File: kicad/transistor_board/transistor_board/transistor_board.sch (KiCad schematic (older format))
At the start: 16 parts, among them Q1 MMBF170, Q2 MMBF170, Q3 MMBF170, U1 DRV8872DDAR, U2 ESP32-cam, U3 LM7805_TO220

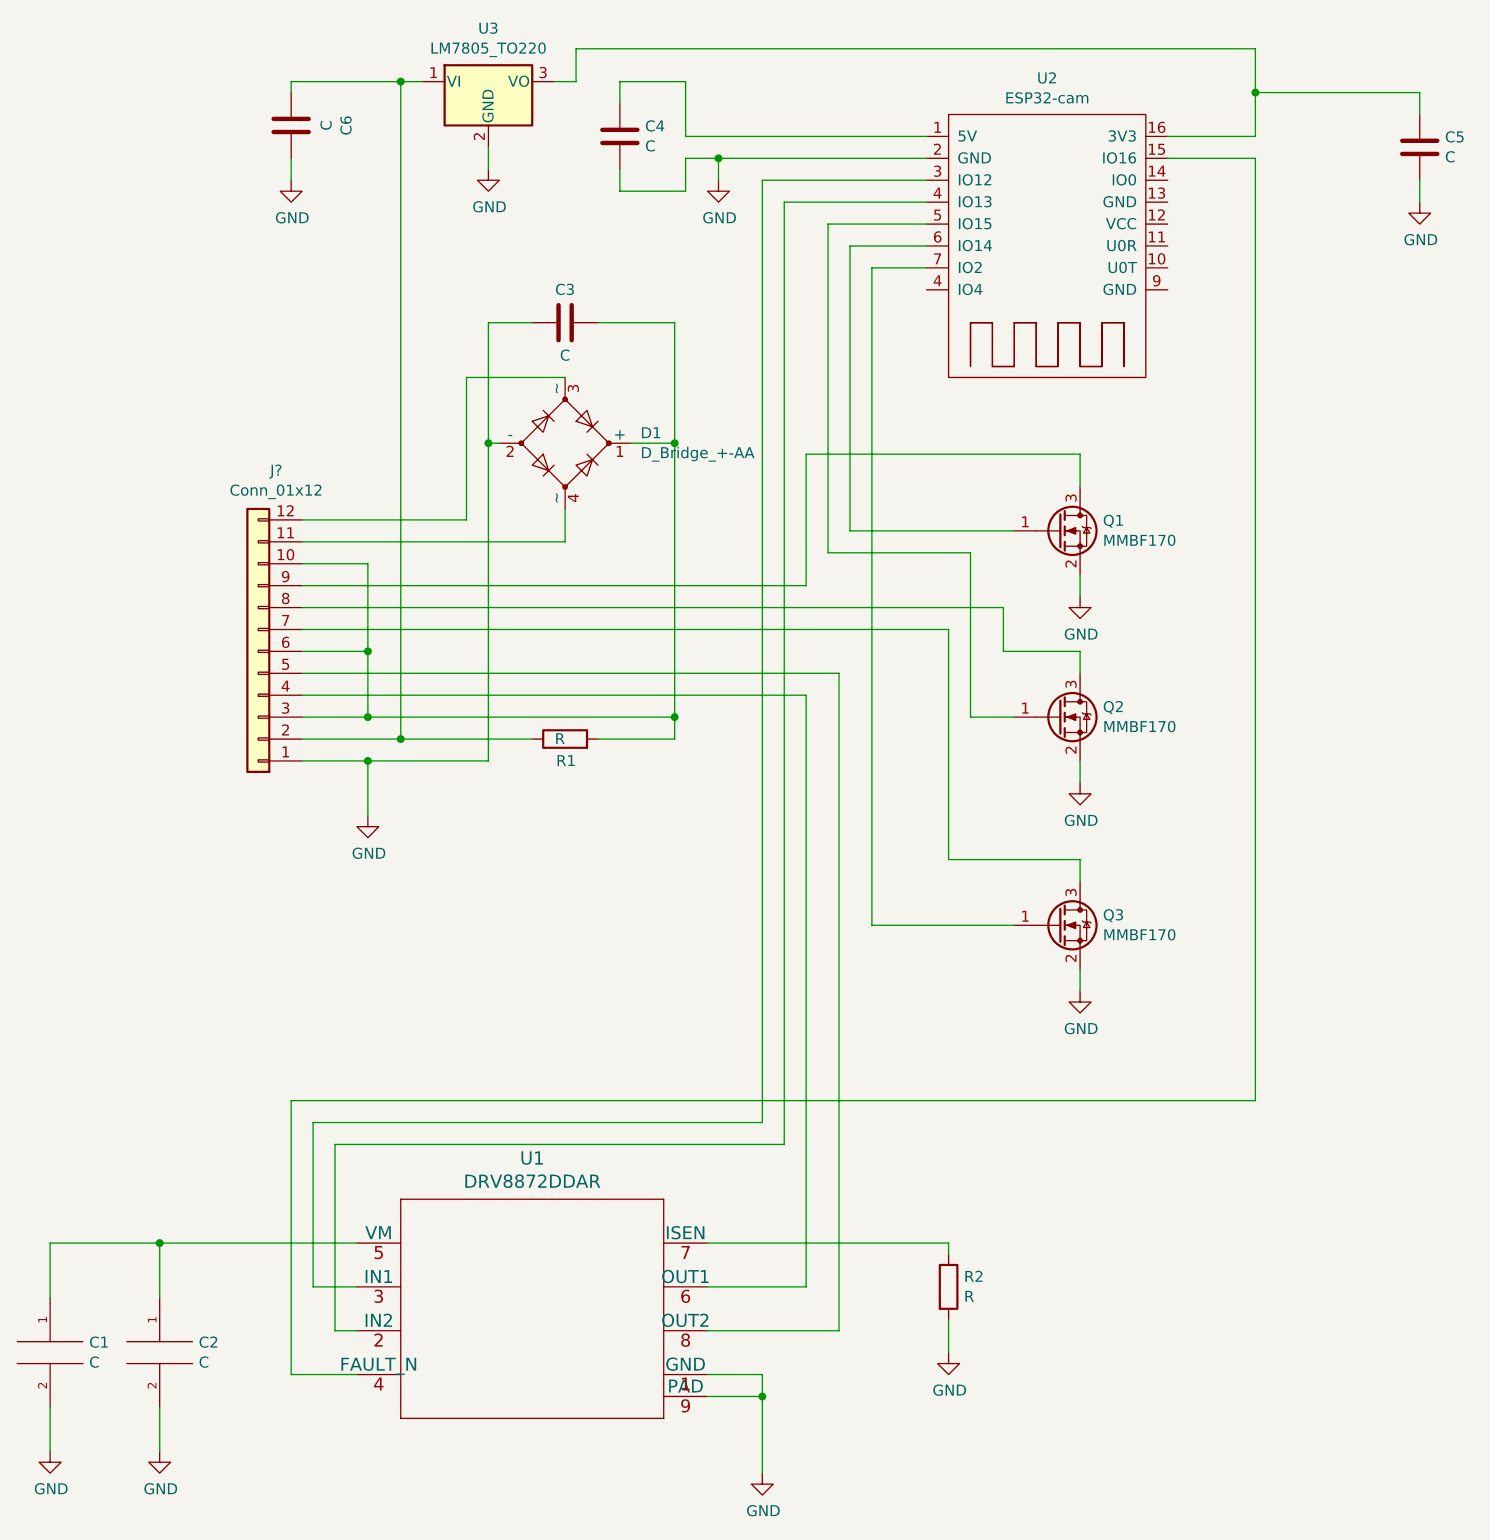
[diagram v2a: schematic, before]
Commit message: motor not powered via resistor
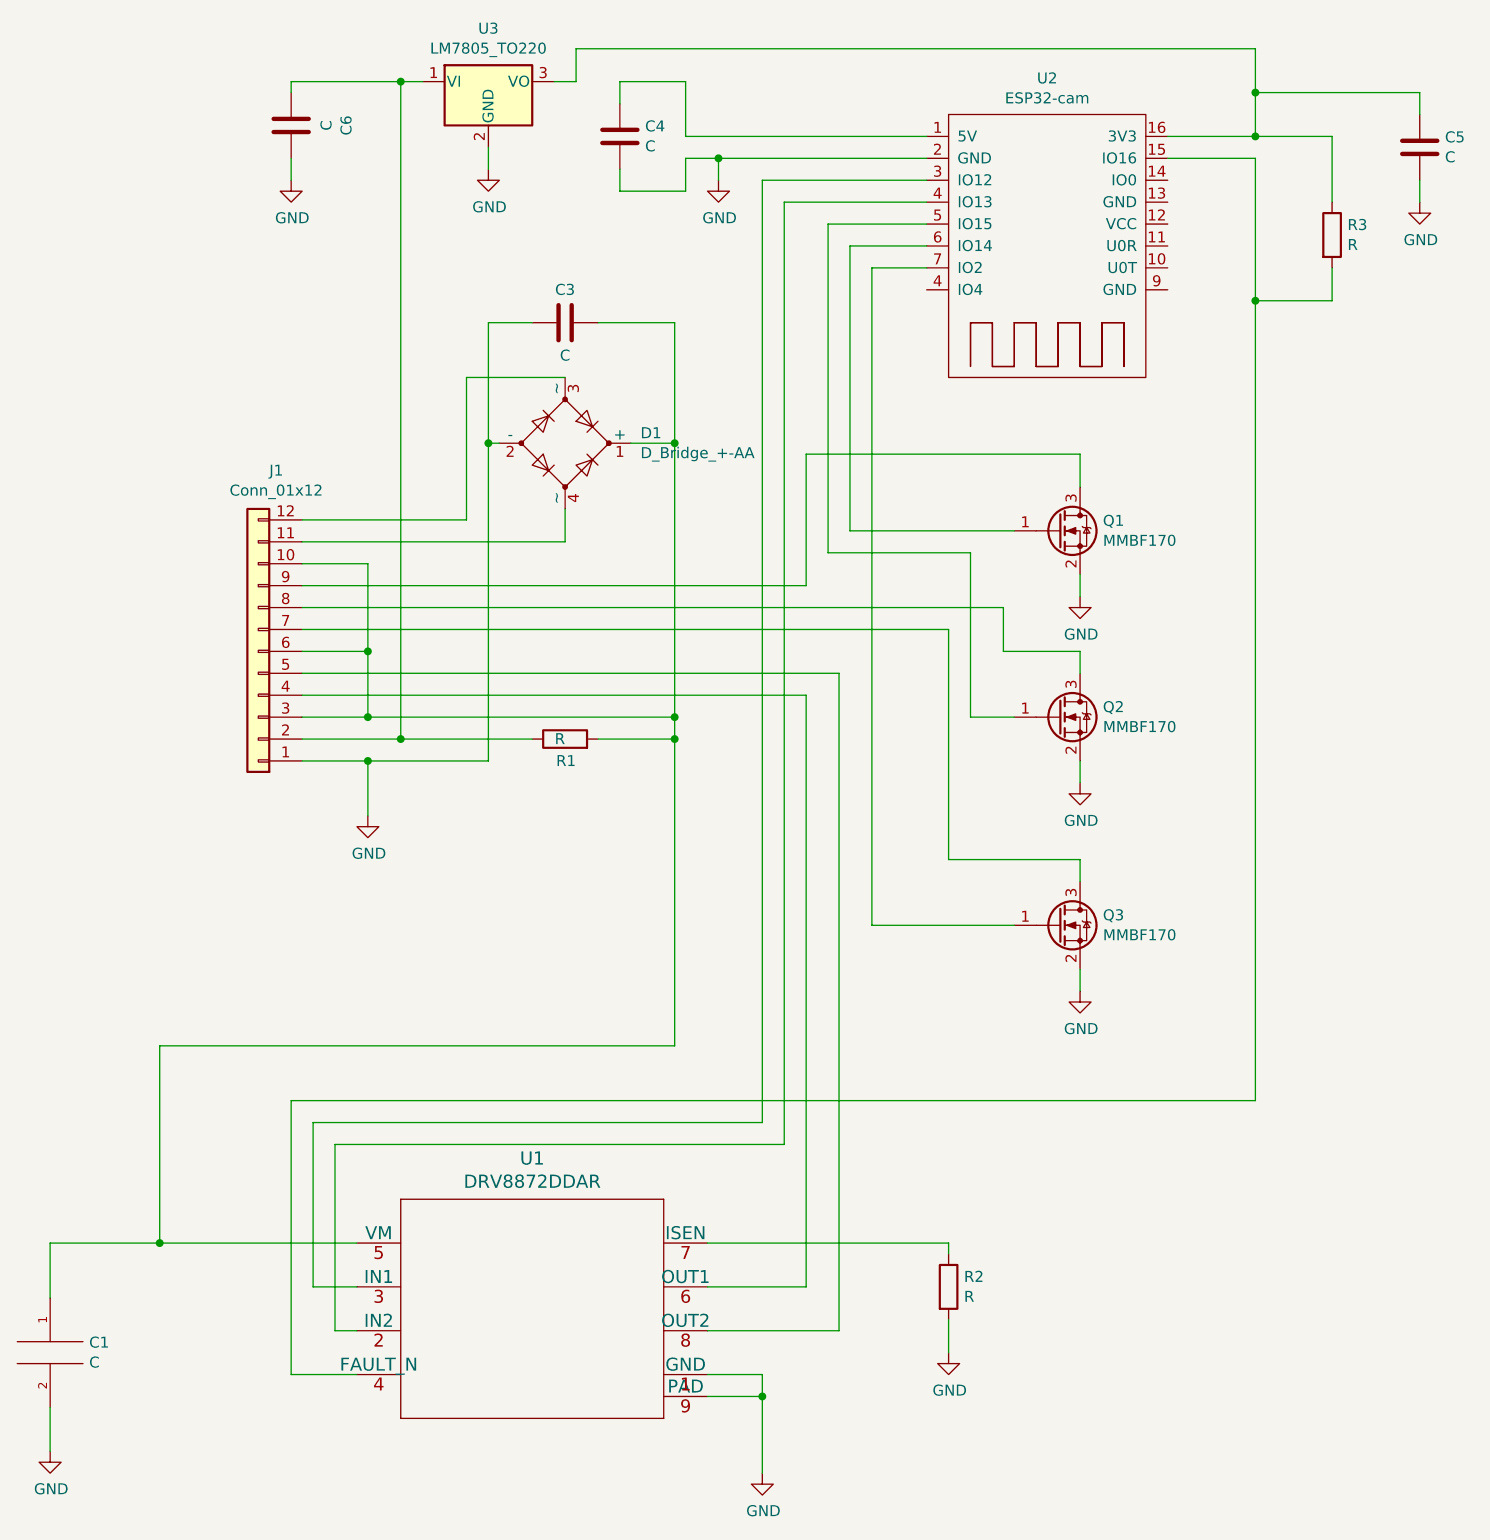
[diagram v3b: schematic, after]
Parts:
- removed C2: C, symbol pspice:C
- added R3: R, symbol Device:R
- gave numbers to parts that had none: 1
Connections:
- net at U1.4 (FAULT_N), U2.15 (IO16): now also R3.2
- net at C5.1, U2.16 (3V3), U3.3 (VO): now also R3.1
- net at U2.4 (IO4): now also U1.2 (IN2)
- net at C3.1, D1.1 (+), J1.10 (Pin_10)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: now also C1.1, U1.5 (VM)
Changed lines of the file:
@@
 	1    0    0    -1
 $EndComp
-$Comp
-L pspice:C C2
-U 1 1 5F221454
-P 3050 6650
-F 0 "C2" H 3228 6696 50  0000 L CNN
-F 1 "C" H 3228 6605 50  0000 L CNN
-F 2 "" H 3050 6650 50  0001 C CNN
-F 3 "~" H 3050 6650 50  0001 C CNN
-	1    3050 6650
-	1    0    0    -1
-$EndComp
-$Comp
-L power:GND #PWR02
-U 1 1 5F22278D
-P 3050 7100
-F 0 "#PWR02" H 3050 6850 50  0001 C CNN
-F 1 "GND" H 3055 6927 50  0000 C CNN
-F 2 "" H 3050 7100 50  0001 C CNN
-F 3 "" H 3050 7100 50  0001 C CNN
-	1    3050 7100
-	1    0    0    -1
-$EndComp
-Wire Wire Line
-	3050 7100 3050 6900
 Wire Wire Line
 	3050 6150 3950 6150
-Wire Wire Line
-	3050 6400 3050 6150
 $Comp
 L pspice:C C1
@@
 	3650 5500 8050 5500
 Wire Wire Line
-	8050 5500 8050 1200
+	8050 5500 8050 1850
 Wire Wire Line
 	8050 1200 7650 1200
@@
 	5400 3750 5400 3850
 $Comp
-L Connector_Generic:Conn_01x12 J?
+L Connector_Generic:Conn_01x12 J1
 U 1 1 5F29655C
 P 3500 3450
-F 0 "J?" H 3418 2625 50  0000 C CNN
+F 0 "J1" H 3418 2625 50  0000 C CNN
 F 1 "Conn_01x12" H 3418 2716 50  0000 C CNN
 F 2 "" H 3500 3450 50  0001 C CNN
@@
 	4000 3450 4000 3050
 Connection ~ 4000 3450
+$Comp
+L Device:R R3
+U 1 1 5F258BB6
+P 8400 1550
+F 0 "R3" H 8470 1596 50  0000 L CNN
+F 1 "R" H 8470 1505 50  0000 L CNN
+F 2 "" V 8330 1550 50  0001 C CNN
+F 3 "~" H 8400 1550 50  0001 C CNN
+	1    8400 1550
+	1    0    0    -1
+$EndComp
+Wire Wire Line
+	8400 1400 8400 1100
+Wire Wire Line
+	8400 1100 8050 1100
+Connection ~ 8050 1100
+Wire Wire Line
+	8400 1700 8400 1850
+Wire Wire Line
+	8400 1850 8050 1850
+Connection ~ 8050 1850
+Wire Wire Line
+	8050 1850 8050 1200
+Wire Wire Line
+	5400 3850 5400 5250
+Wire Wire Line
+	5400 5250 3050 5250
+Wire Wire Line
+	3050 5250 3050 6150
+Connection ~ 5400 3850
 $EndSCHEMATC
